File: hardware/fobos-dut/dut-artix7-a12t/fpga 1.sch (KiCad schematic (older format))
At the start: 34 parts, among them J1 Target, J2 Pmod 2x6, U2 SP3003-04ATG, U3 SP3003-04ATG, U4 SP3003-04ATG, U7 TS3A27518EIPWRQ1

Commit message: -Added TS3A27518EIPWRQ1 6 circuit analog SPDT switch -Connected tripple output power supply to FPGA power pins -Added bypass and decoupling capacitors to the FPGA power pins(these will be DNP) -Swapped out the old bulky banana jack socket parts for 1050752001 and 1050753001 -Added JTAG header -Added test loops -Added boot mode dip switch -Swapped out the right angle 0.1" headers for vertical 0.1" headers(personal preference) -Working my way through the 7_series_schematic_review_recommendations spreadsheet
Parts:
- removed C1, C2, C3, C54: 100nF, Capacitor_SMD:C_0603_1608Metric, symbol Device:C
- removed J1: Target, Connector_IDC:IDC-Header_2x10_P2.54mm_Horizontal, symbol Connector_Generic:Conn_02x10_Odd_Even
- removed J2: Pmod 2x6, symbol Connector_Generic:Conn_02x06_Top_Bottom
- removed R1, R13, R14, R15, R16, R17, R18, R2, R3, R4, R5, R6: 22R, Resistor_SMD:R_0603_1608Metric, symbol Device:R
- removed R10, R11, R12, R19, R20, R7, R8, R9: 200R, Resistor_SMD:R_0603_1608Metric, symbol Device:R
- removed R51: 10KR, Resistor_SMD:R_0603_1608Metric, symbol Device:R
- removed TP2, TP3, TP4: 5281, cerg:5281, symbol cerg:5281
- removed U2, U3, U4: SP3003-04ATG, Package_SO:MSOP-10_3x3mm_P0.5mm, symbol cerg:SP3003-04ATG
- removed U7: TS3A27518EIPWRQ1, Package_SO:TSSOP-24_4.4x7.8mm_P0.65mm, symbol cerg:TS3A27518EIPWRQ1
- added C16: 100n, Capacitor_SMD:C_0603_1608Metric, symbol Device:C
- added R25: 4K7, Resistor_SMD:R_0603_1608Metric, symbol Device:R
- added R26, R27, R28: 33R, Resistor_SMD:R_0603_1608Metric, symbol Device:R
- added R29, R30: 1R, Resistor_SMD:R_0603_1608Metric, symbol Device:R
- added U1: XC7A12T-CSG325, Package_BGA:Xilinx_CSG325, symbol cerg:XC7A12T-CSG325
- added U9: IS25LP256D-JMLE, Package_SO:SOIC-16W_7.5x10.3mm_P1.27mm, symbol cerg:IS25LP256D-JMLE
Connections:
- net labels added: FPGA_CCLK, HOLD, WP
- net labels removed: (Aux)FC_PROG, (Ready)FC2D_HS, (Valid)FD2C_HS, CW_HS1, CW_HS2, CW_MISO, CW_MOSI, CW_PDIC, CW_PDID, CW_RST, CW_SCK, CW_TARG1, CW_TARG2, CW_TARG3, CW_TARG4, FC2D_CLK, FC2D_HS, FC_3V3, FC_5V, FC_DIO0, FC_DIO0_MUX, FC_DIO1, FC_DIO1_MUX, FC_DIO2, FC_DIO2_MUX, FC_DIO3, FC_DIO3_MUX, FC_IO, FC_PROG, FC_RST, FD2C_CLK, FD2C_HS, FD_TF, FD_VREF, SW_CLK, SW_DIN, SW_DONE, SW_INIT_B, SW_PROGRAM_B
- wire segments 169 -> 40
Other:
- note added: "JA can be \ndifferentially\nrouted"
- note removed: "ESD Protection"
- note removed: "FOBOS Target Connector"
- note removed: "FPGA\nPin"
- note removed: "PMOD Connector"
- note removed: "Programming/DUT Communication Switches"

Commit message: Schematic is 99% complete, getting started on layout
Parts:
- removed R29: 1R, Resistor_SMD:R_0603_1608Metric, symbol Device:R
- added R52: 4.7KR, Resistor_SMD:R_0603_1608Metric, symbol Device:R
- added R56: 33R, Resistor_SMD:R_0603_1608Metric, symbol Device:R
- R25: value 4K7 -> 4.7KR
- R26: value 33R -> 4.7KR
- R30: value 1R -> 0R
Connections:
- net labels added: +3V3, SW_CLK, SW_DIN
- net labels removed: FPGA_CCLK, HOLD, VCCIO, WP
- wire segments 40 -> 47
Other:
- moved on the sheet: C16, R25

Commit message: ARTIX 7 DUT Layout is 80% done
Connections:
- net labels added: USER_BTN_1, USER_BTN_2, USER_LED_1, USER_LED_2, USER_LED_3, USER_LED_4
- wire segments 47 -> 53
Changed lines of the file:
@@
 EndData
 $EndBitmap
-Text GLabel 4050 2800 0    50   Input ~ 0
+Text GLabel 7950 3000 2    50   Input ~ 0
 JA1
-Text GLabel 4050 2900 0    50   Input ~ 0
+Text GLabel 7950 3600 2    50   Input ~ 0
 JA7
-Text GLabel 4050 3200 0    50   Input ~ 0
+Text GLabel 7950 2900 2    50   Input ~ 0
 JA2
-Text GLabel 4050 3300 0    50   Input ~ 0
+Text GLabel 7950 3400 2    50   Input ~ 0
 JA8
-Text GLabel 4050 3400 0    50   Input ~ 0
+Text GLabel 7950 3100 2    50   Input ~ 0
 JA3
-Text GLabel 4050 3500 0    50   Input ~ 0
+Text GLabel 7950 3500 2    50   Input ~ 0
 JA9
-Text GLabel 4050 3800 0    50   Input ~ 0
+Text GLabel 7950 3200 2    50   Input ~ 0
 JA4
-Text GLabel 4100 3900 0    50   Input ~ 0
-JA10
-Wire Wire Line
-	4050 2800 4300 2800
-Wire Wire Line
-	4300 2900 4050 2900
-Wire Wire Line
-	4300 3200 4050 3200
-Wire Wire Line
-	4050 3300 4300 3300
-Wire Wire Line
-	4050 3400 4300 3400
-Wire Wire Line
-	4050 3500 4300 3500
-Wire Wire Line
-	4050 3800 4300 3800
-Wire Wire Line
-	4100 3900 4300 3900
-Text Notes 3350 3950 0    50   ~ 0
+Wire Wire Line
+	7950 3000 7700 3000
+Wire Wire Line
+	7700 3600 7950 3600
+Wire Wire Line
+	7700 2900 7950 2900
+Wire Wire Line
+	7950 3400 7700 3400
+Wire Wire Line
+	7950 3100 7700 3100
+Wire Wire Line
+	7950 3500 7700 3500
+Wire Wire Line
+	7950 3200 7700 3200
+Text Notes 8200 3250 0    50   ~ 0
 JA can be \ndifferentially\nrouted
 $Comp
@@
 Wire Wire Line
 	3100 1550 3100 1700
+Text GLabel 7900 3300 2    50   Input ~ 0
+JA10
+Wire Wire Line
+	7900 3300 7700 3300
+Text GLabel 7950 3900 2    50   Input ~ 0
+USER_LED_4
+Wire Wire Line
+	7700 3900 7950 3900
+Text GLabel 7950 4000 2    50   Input ~ 0
+USER_LED_3
+Wire Wire Line
+	7700 4000 7950 4000
+Text GLabel 7950 4200 2    50   Input ~ 0
+USER_LED_2
+Wire Wire Line
+	7700 4200 7950 4200
+Text GLabel 7950 4100 2    50   Input ~ 0
+USER_LED_1
+Wire Wire Line
+	7700 4100 7950 4100
+Text GLabel 7950 4800 2    50   Input ~ 0
+USER_BTN_2
+Wire Wire Line
+	7950 4800 7700 4800
+Text GLabel 7950 4700 2    50   Input ~ 0
+USER_BTN_1
+Wire Wire Line
+	7950 4700 7700 4700
 $EndSCHEMATC

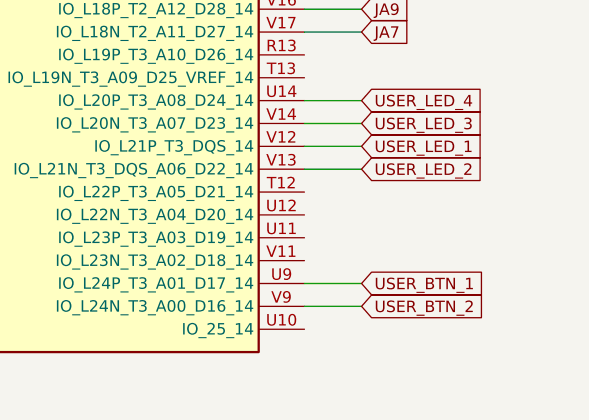
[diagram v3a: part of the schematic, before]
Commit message: Completed layout of the Artix 7 DUT Board
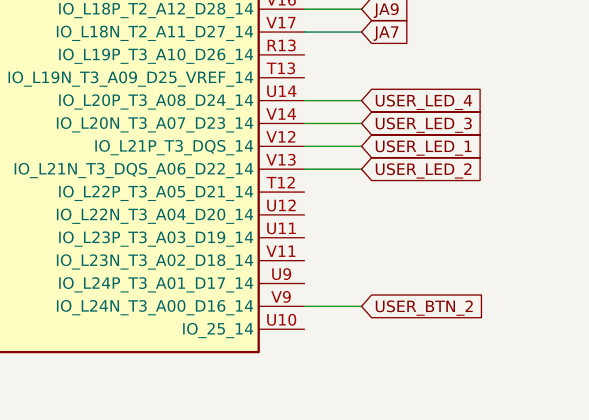
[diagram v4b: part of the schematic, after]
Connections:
- net labels removed: USER_BTN_1
- wire segments 53 -> 52
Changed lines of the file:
@@
 Wire Wire Line
 	7950 4800 7700 4800
-Text GLabel 7950 4700 2    50   Input ~ 0
-USER_BTN_1
-Wire Wire Line
-	7950 4700 7700 4700
 $EndSCHEMATC

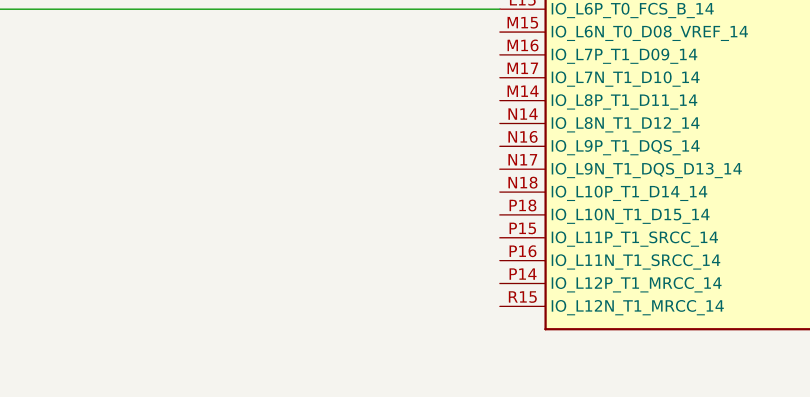
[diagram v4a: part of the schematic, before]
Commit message: Added external 5V connector Added shunt for FC3v3 and 3V3 Added silkscreen which clarifies switch functionality Thickened 5 mil traces to 7 mil where feasible Moved Vcore amplifier closer to Vcore pad to reduce amplification of noise
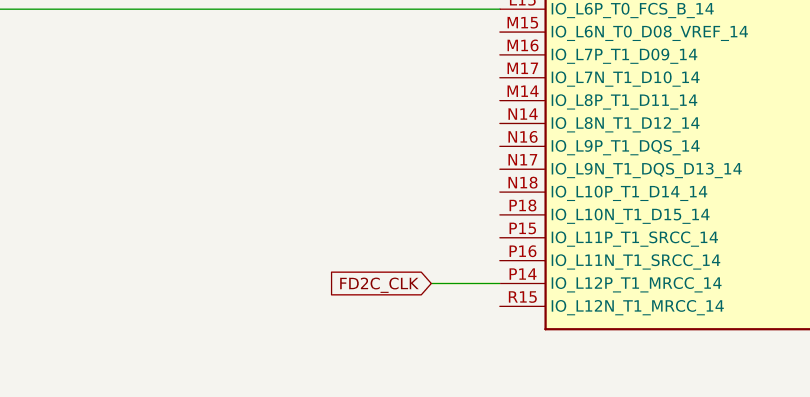
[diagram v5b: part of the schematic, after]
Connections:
- net labels added: FD2C_CLK
- wire segments 52 -> 53
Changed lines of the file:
@@
 Wire Wire Line
 	7950 4800 7700 4800
+Text GLabel 4000 4800 0    50   Input ~ 0
+FD2C_CLK
+Wire Wire Line
+	4300 4800 4000 4800
 $EndSCHEMATC

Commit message: Added Manufacturer Part Number, Manufacturer to all components except ferrite beads Added digikey quote
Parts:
- C16: value 100n -> 100nF; Description (none) -> CAP CER 0.1UF 6.3V X7R 0603; MPN (none) -> 06036C104KAT4A; Manufacturer (none) -> AVX Corporation
- R25, R26, R52: Description (none) -> RES SMD 4.7K OHM 5% 1/10W 0603; MPN (none) -> ERJ-3GEYJ472V; Manufacturer (none) -> Panasonic Electronic Components
- R27, R28, R56: Description (none) -> RES SMD 33 OHM 0.5% 1/10W 0603; MPN (none) -> ERA-3AHD330V; Manufacturer (none) -> Panasonic Electronic Components
- R30: Description (none) -> RES 0 OHM JUMPER 1/10W 0603; MPN (none) -> RMCF0603ZT0R00; Manufacturer (none) -> Stackpole Electronics Inc
- U1: Description (none) -> IC FPGA 150 I/O 324CSBGA; MPN (none) -> XC7A12T-2CSG325I; Manufacturer (none) -> Xilinx Inc.
- U9: Description (none) -> IC FLASH 256MBIT SPI/QUAD 16SOIC; Manufacturer (none) -> ISSI, Integrated Silicon Solution Inc
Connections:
- net labels removed: FD2C_CLK
- wire segments 53 -> 52
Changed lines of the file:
@@
 F 2 "Package_BGA:Xilinx_CSG325" H 6000 3700 50  0001 C CNN
 F 3 "https://www.xilinx.com/support/documentation/data_sheets/ds180_7Series_Overview.pdf" H 6000 3700 50  0001 C CNN
+F 4 "IC FPGA 150 I/O 324CSBGA" H 6000 3700 50  0001 C CNN "Description"
+F 5 "XC7A12T-2CSG325I" H 6000 3700 50  0001 C CNN "MPN"
+F 6 "Xilinx Inc." H 6000 3700 50  0001 C CNN "Manufacturer"
 	2    6000 3700
 	1    0    0    -1
@@
 F 2 "Resistor_SMD:R_0603_1608Metric" V 3530 2700 50  0001 C CNN
 F 3 "~" H 3600 2700 50  0001 C CNN
+F 4 "RES SMD 33 OHM 0.5% 1/10W 0603" H 3600 2700 50  0001 C CNN "Description"
+F 5 "ERA-3AHD330V" H 3600 2700 50  0001 C CNN "MPN"
+F 6 "Panasonic Electronic Components" H 3600 2700 50  0001 C CNN "Manufacturer"
 	1    3600 2700
 	0    1    1    0
@@
 F 2 "Resistor_SMD:R_0603_1608Metric" V 3530 2500 50  0001 C CNN
 F 3 "~" H 3600 2500 50  0001 C CNN
+F 4 "RES SMD 33 OHM 0.5% 1/10W 0603" H 3600 2500 50  0001 C CNN "Description"
+F 5 "ERA-3AHD330V" H 3600 2500 50  0001 C CNN "MPN"
+F 6 "Panasonic Electronic Components" H 3600 2500 50  0001 C CNN "Manufacturer"
 	1    3600 2500
 	0    1    1    0
@@
 F 2 "Resistor_SMD:R_0603_1608Metric" V 880 2150 50  0001 C CNN
 F 3 "~" H 950 2150 50  0001 C CNN
+F 4 "RES SMD 4.7K OHM 5% 1/10W 0603" H 950 2150 50  0001 C CNN "Description"
+F 5 "ERJ-3GEYJ472V" H 950 2150 50  0001 C CNN "MPN"
+F 6 "Panasonic Electronic Components" H 950 2150 50  0001 C CNN "Manufacturer"
 	1    950  2150
 	-1   0    0    1
@@
 F 2 "Resistor_SMD:R_0603_1608Metric" V 4080 1700 50  0001 C CNN
 F 3 "~" H 4150 1700 50  0001 C CNN
+F 4 "RES 0 OHM JUMPER 1/10W 0603" H 4150 1700 50  0001 C CNN "Description"
+F 5 "RMCF0603ZT0R00" H 4150 1700 50  0001 C CNN "MPN"
+F 6 "Stackpole Electronics Inc" H 4150 1700 50  0001 C CNN "Manufacturer"
 	1    4150 1700
 	0    1    1    0
@@
 F 3 "https://www.digikey.com/en/products/detail/issi-integrated-silicon-solution-inc/IS25LP256D-JMLE/7567432" H 2000 2200 50  0001 C CNN
 F 4 "IS25LP256D-JMLE" H 2000 2200 50  0001 C CNN "MPN"
+F 5 "IC FLASH 256MBIT SPI/QUAD 16SOIC" H 2000 2200 50  0001 C CNN "Description"
+F 6 "ISSI, Integrated Silicon Solution Inc" H 2000 2200 50  0001 C CNN "Manufacturer"
 	1    2000 2200
 	1    0    0    -1
@@
 P 3100 1850
 F 0 "C16" H 3215 1896 50  0000 L CNN
-F 1 "100n" H 3215 1805 50  0000 L CNN
+F 1 "100nF" H 3215 1805 50  0000 L CNN
 F 2 "Capacitor_SMD:C_0603_1608Metric" H 3138 1700 50  0001 C CNN
 F 3 "~" H 3100 1850 50  0001 C CNN
+F 4 "CAP CER 0.1UF 6.3V X7R 0603" H 3100 1850 50  0001 C CNN "Description"
+F 5 "06036C104KAT4A" H 3100 1850 50  0001 C CNN "MPN"
+F 6 "AVX Corporation" H 3100 1850 50  0001 C CNN "Manufacturer"
 	1    3100 1850
 	1    0    0    -1
@@
 F 2 "Resistor_SMD:R_0603_1608Metric" V 1480 2150 50  0001 C CNN
 F 3 "~" H 1550 2150 50  0001 C CNN
+F 4 "RES SMD 4.7K OHM 5% 1/10W 0603" H 1550 2150 50  0001 C CNN "Description"
+F 5 "ERJ-3GEYJ472V" H 1550 2150 50  0001 C CNN "MPN"
+F 6 "Panasonic Electronic Components" H 1550 2150 50  0001 C CNN "Manufacturer"
 	1    1550 2150
 	-1   0    0    1
@@
 F 2 "Resistor_SMD:R_0603_1608Metric" V 1180 2150 50  0001 C CNN
 F 3 "~" H 1250 2150 50  0001 C CNN
+F 4 "RES SMD 4.7K OHM 5% 1/10W 0603" H 1250 2150 50  0001 C CNN "Description"
+F 5 "ERJ-3GEYJ472V" H 1250 2150 50  0001 C CNN "MPN"
+F 6 "Panasonic Electronic Components" H 1250 2150 50  0001 C CNN "Manufacturer"
 	1    1250 2150
 	-1   0    0    1
@@
 F 2 "Resistor_SMD:R_0603_1608Metric" V 3530 2300 50  0001 C CNN
 F 3 "~" H 3600 2300 50  0001 C CNN
+F 4 "RES SMD 33 OHM 0.5% 1/10W 0603" H 3600 2300 50  0001 C CNN "Description"
+F 5 "ERA-3AHD330V" H 3600 2300 50  0001 C CNN "MPN"
+F 6 "Panasonic Electronic Components" H 3600 2300 50  0001 C CNN "Manufacturer"
 	1    3600 2300
 	0    1    1    0
@@
 Wire Wire Line
 	7950 4800 7700 4800
-Text GLabel 4000 4800 0    50   Input ~ 0
-FD2C_CLK
-Wire Wire Line
-	4300 4800 4000 4800
 $EndSCHEMATC
